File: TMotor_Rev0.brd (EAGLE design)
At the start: 59.7 x 78.4 mm, 37 parts, among them U1 INA125U, U2 INA125U

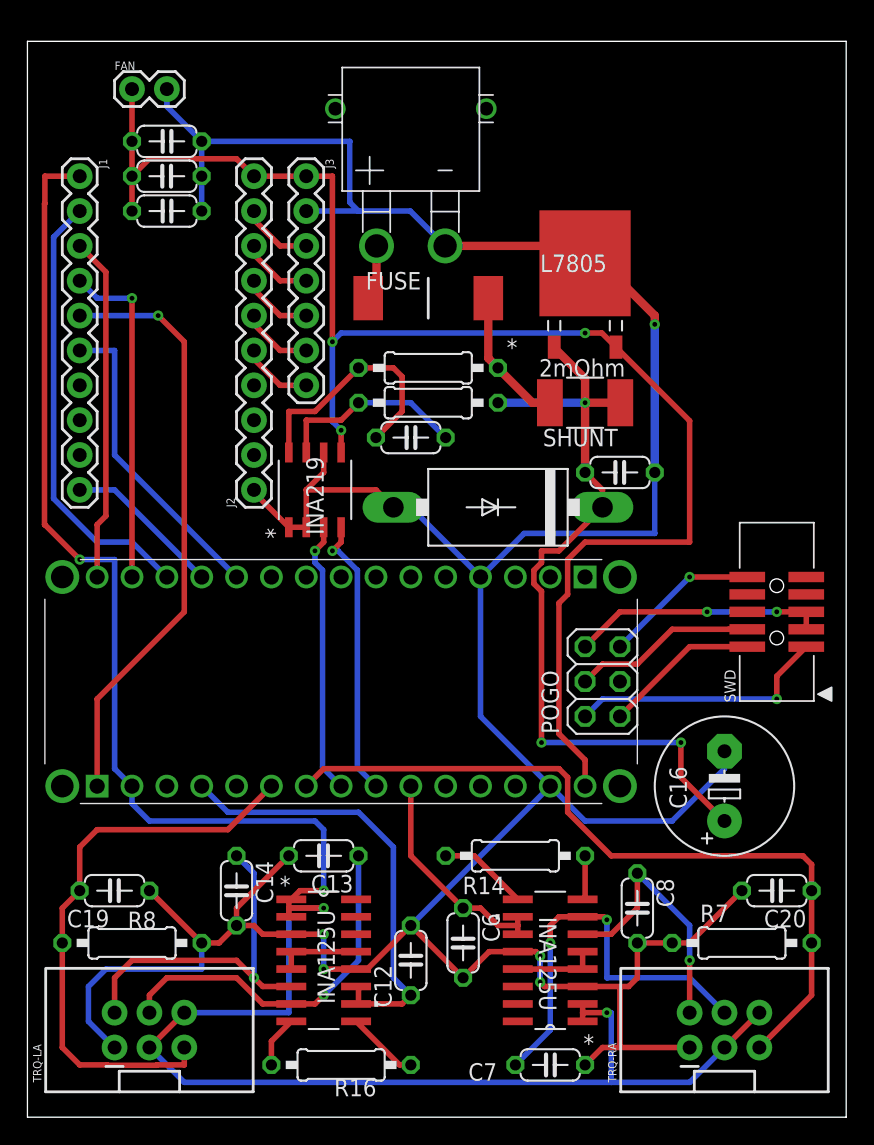
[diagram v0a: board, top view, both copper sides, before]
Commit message: Rearranged pre ground plane pour
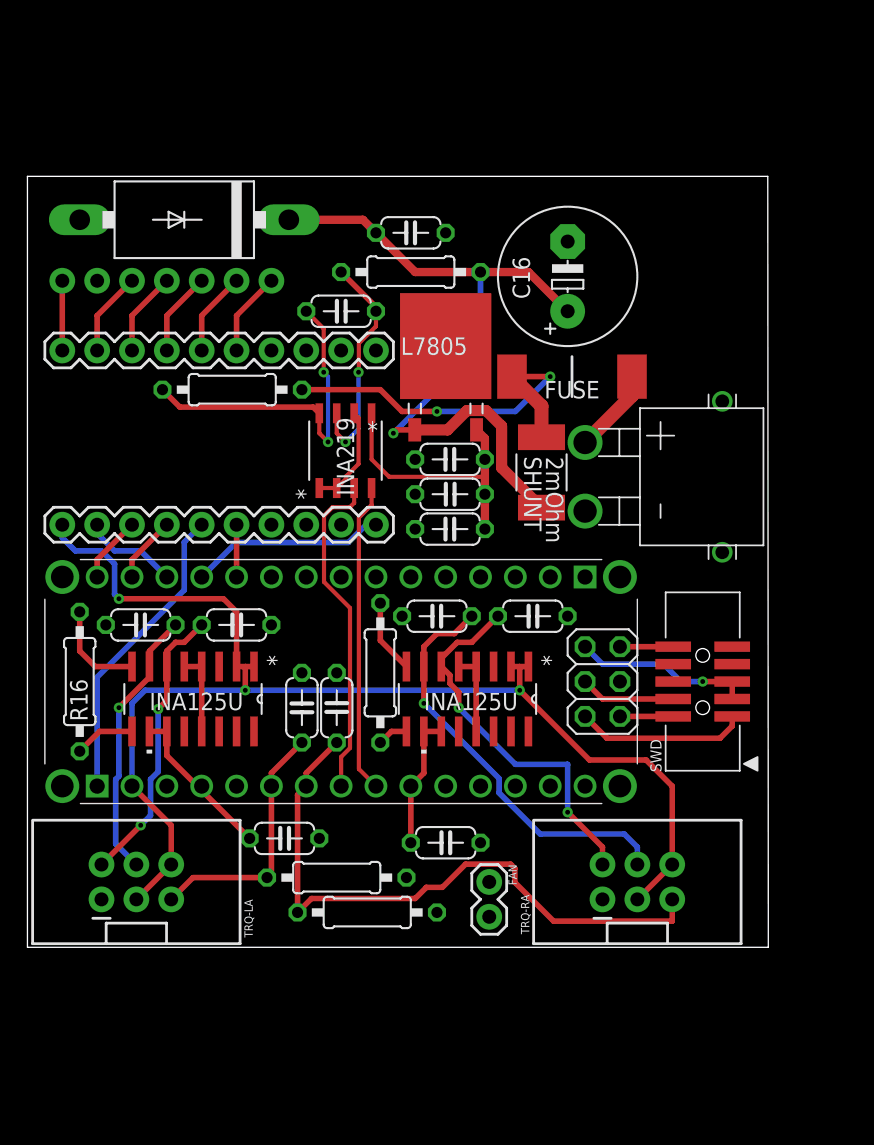
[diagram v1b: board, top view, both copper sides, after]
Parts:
- moved FAN 63.4 mm to (33.7, 13.3), turned to 270 degrees
- moved C16 38.9 mm to (39.4, 57.5)
- moved C20 34.7 mm to (22.5, 26.0), turned to 90 degrees
- moved R16 33.8 mm to (3.81, 27.9), turned to 270 degrees
- moved C7 33.7 mm to (29.8, 32.7), turned to 180 degrees
- moved C15 31.0 mm to (30.8, 44.1), turned to 180 degrees
- moved C3 31.0 mm to (30.8, 41.6), turned to 0 degrees
- moved C5 31.0 mm to (30.8, 39.1), turned to 180 degrees
- moved D1 31.0 mm to (11.4, 61.6)
- moved R7 27.4 mm to (24.8, 11.1), turned to 180 degrees
- moved J1 25.4 mm to (2.54, 39.4), turned to 0 degrees
- moved C4 23.2 mm to (27.9, 60.6)
- moved C8 22.6 mm to (36.8, 32.7), turned to 0 degrees
- moved C13 21.5 mm to (8.26, 32.1)
- moved U1 21.3 mm to (12.1, 26.7), turned to 270 degrees
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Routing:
- net GND: track 260.0 -> 7.51 mm, vias 5 -> 0
- net VIN: track 109.7 -> 24.7 mm, vias 3 -> 0
- net 3.3V: track 155.6 -> 95.7 mm, vias 4 -> 3
- net CAN_CS: track 32.4 -> 7.03 mm
- net A2: track 41.6 -> 18.5 mm
- net SCK: track 43.4 -> 22.2 mm, vias 1 -> 0
- net A0: track 32.7 -> 11.8 mm
- net MISO: track 25.2 -> 4.86 mm
- net MOSI: track 24.7 -> 4.86 mm, vias 1 -> 0
- net CAN_INT: track 22.7 -> 3.81 mm
- net PF_VCC: track 10.2 -> 27.9 mm, vias 0 -> 2
- net A3: track 56.7 -> 46.2 mm
- net N$8: track 19.1 -> 27.5 mm, vias 1 -> 2
- net SWDIO: track 11.4 -> 3.88 mm
- net NRESET: track 11.4 -> 3.88 mm, vias 1 -> 0
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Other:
- board size 59.7 x 78.4 mm -> 54 x 56.2 mm

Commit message: Post ground plane and DRC
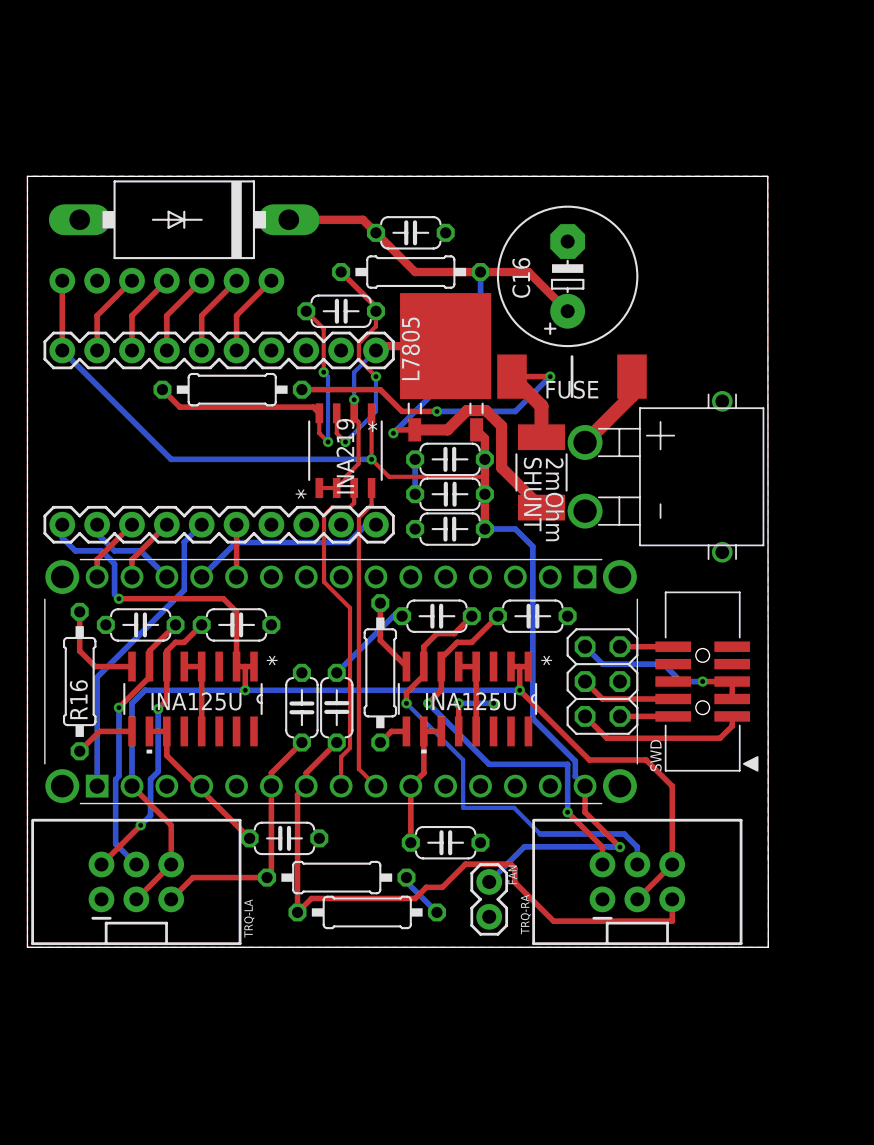
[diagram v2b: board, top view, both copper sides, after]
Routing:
- net VIN: track 24.7 -> 89.7 mm, vias 0 -> 2
- net GND: track 7.51 -> 35.0 mm, vias 0 -> 3
- net N$9: track 30.3 -> 33.8 mm
- net N$8: track 27.5 -> 29.4 mm
- net N$26: track 16.7 -> 17.7 mm
- added copper zone on layer 1, net GND

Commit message: Fixed power electronics, pre Paul PCB changes.
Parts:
- moved C15 27.7 mm to (33.3, 16.5)
- moved L7805 21.5 mm to (51.4, 47.6), turned to 270 degrees
- moved C4 21.2 mm to (47.6, 52.7)
- moved U$9 20.1 mm to (36.8, 62.5), turned to 0 degrees
- moved R2 18.4 mm to (33.0, 52.4)
- moved C5 17.2 mm to (47.6, 42.5), turned to 0 degrees
- moved D1 16.9 mm to (28.3, 63.5), flipped to the bottom, turned to 90 degrees
- moved R1 14.6 mm to (38.1, 47.3)
- moved SHUNT 10.7 mm to (41.0, 53.3)
- moved INA219 10.7 mm to (33.7, 42.5)
- moved C16 10.4 mm to (48.9, 61.6), turned to 0 degrees
- moved C9 9.34 mm to (30.5, 49.5)
- moved FUSE 9.25 mm to (37.1, 59.1), turned to 180 degrees
- moved C3 7.36 mm to (38.1, 42.5), turned to 90 degrees
- moved C6 4.77 mm to (25.7, 16.5)
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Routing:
- net PF_VCC: track 27.9 -> 8.88 mm, vias 2 -> 0
- net L7_VIN: track 53.6 -> 35.4 mm, vias 1 -> 0
- net N$23: track 24.7 -> 8.70 mm, vias 2 -> 0
- net N$26: track 17.7 -> 4.26 mm, vias 2 -> 0
- net GND: track 35.0 -> 22.0 mm, vias 3 -> 2
- net VIN: track 89.7 -> 98.6 mm, vias 2 -> 0
- net SCL1: track 22.6 -> 30.2 mm
- net SDA1: track 24.4 -> 31.8 mm
- net A6: track 9.78 -> 12.0 mm
- net VCC: track 6.22 -> 4.14 mm
- net NRESET: track 3.88 -> 5.89 mm
- net SW3.3V: track 12.5 -> 14.1 mm
- net SWDIO: track 3.88 -> 5.33 mm
- net 3.3V: track 95.7 -> 96.3 mm
- net SCK: track 22.2 -> 22.8 mm
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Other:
- board size 54 x 56.2 mm -> 56.5 x 66.3 mm

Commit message: Forgot to save haha
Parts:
- moved SWD 0.63 mm to (49.8, 31.4)
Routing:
- net SWGND: track 13.4 -> 14.1 mm
- net SWDIO: track 5.33 -> 5.96 mm
- net SWCLK: track 7.34 -> 7.98 mm
- net NRESET: track 5.89 -> 6.52 mm
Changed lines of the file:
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@@
 <attribute name="MOUSER_PRICE-STOCK" value="https://www.mouser.co.uk/ProductDetail/Arduino/ABX00028/?qs=PzGy0jfpSMtit6rnFl8mVg%3D%3D" x="58.42" y="17.78" size="1.778" layer="27" display="off"/>
 </element>
-<element name="SWD" library="microbuilder" package="2X05_1.27MM_BOX_POSTS" value="20317" x="49.2125" y="31.4325" smashed="yes" rot="R90">
-<attribute name="NAME" x="46.2125" y="24.8325" size="0.8128" layer="25" ratio="18" rot="R90"/>
-<attribute name="VALUE" x="51.6125" y="25.3325" size="0.4064" layer="27" ratio="10" rot="R90"/>
+<element name="SWD" library="microbuilder" package="2X05_1.27MM_BOX_POSTS" value="20317" x="49.8475" y="31.4325" smashed="yes" rot="R90">
+<attribute name="NAME" x="46.8475" y="24.8325" size="0.8128" layer="25" ratio="18" rot="R90"/>
+<attribute name="VALUE" x="52.2475" y="25.3325" size="0.4064" layer="27" ratio="10" rot="R90"/>
 </element>
 <element name="POGO" library="pinhead" library_urn="urn:adsk.eagle:library:325" package="2X03" package3d_urn="urn:adsk.eagle:package:22462/2" value="" x="41.91" y="27.94" smashed="yes" rot="R90">
@@
 <contactref element="POGO" pad="4"/>
 <contactref element="SWD" pad="4"/>
-<wire x1="47.0625" y1="30.1625" x2="45.7925" y2="30.1625" width="0.4064" layer="1"/>
+<wire x1="47.6975" y1="30.1625" x2="45.7925" y2="30.1625" width="0.4064" layer="1"/>
 <wire x1="45.7925" y1="30.1625" x2="44.84" y2="29.21" width="0.4064" layer="1"/>
 <wire x1="44.84" y1="29.21" x2="41.91" y2="29.21" width="0.4064" layer="1"/>
@@
 <contactref element="SWD" pad="5"/>
 <wire x1="40.64" y1="30.48" x2="41.91" y2="29.21" width="0.4064" layer="16"/>
-<wire x1="49.2125" y1="31.4325" x2="47.625" y2="31.4325" width="0.4064" layer="16"/>
+<wire x1="49.8475" y1="31.4325" x2="47.625" y2="31.4325" width="0.4064" layer="16"/>
 <wire x1="47.625" y1="31.4325" x2="45.4025" y2="29.21" width="0.4064" layer="16"/>
 <wire x1="45.4025" y1="29.21" x2="41.91" y2="29.21" width="0.4064" layer="16"/>
-<via x="49.2125" y="31.4325" extent="1-16" drill="0.35"/>
-<wire x1="51.3625" y1="31.4325" x2="49.2125" y2="31.4325" width="0.4064" layer="1"/>
-<wire x1="51.3625" y1="31.4325" x2="51.3625" y2="30.1625" width="0.4064" layer="1"/>
+<via x="49.8475" y="31.4325" extent="1-16" drill="0.35"/>
+<wire x1="51.9975" y1="31.4325" x2="49.8475" y2="31.4325" width="0.4064" layer="1"/>
+<wire x1="51.9975" y1="31.4325" x2="51.9975" y2="30.1625" width="0.4064" layer="1"/>
 </signal>
 <signal name="SW3.3V">
@@
 <wire x1="40.64" y1="25.4" x2="42.2275" y2="23.8125" width="0.4064" layer="1"/>
 <wire x1="42.2275" y1="23.8125" x2="47.3075" y2="23.8125" width="0.4064" layer="1"/>
-<wire x1="47.3075" y1="23.8125" x2="51.3625" y2="27.8675" width="0.4064" layer="1"/>
-<wire x1="51.3625" y1="27.8675" x2="51.3625" y2="28.8925" width="0.4064" layer="1"/>
+<wire x1="47.3075" y1="23.8125" x2="51.9975" y2="28.5025" width="0.4064" layer="1"/>
+<wire x1="51.9975" y1="28.5025" x2="51.9975" y2="28.8925" width="0.4064" layer="1"/>
 </signal>
 <signal name="NRESET">
 <contactref element="POGO" pad="5"/>
 <contactref element="SWD" pad="10"/>
-<wire x1="47.0625" y1="33.9725" x2="45.72" y2="33.9725" width="0.4064" layer="1"/>
+<wire x1="47.6975" y1="33.9725" x2="45.72" y2="33.9725" width="0.4064" layer="1"/>
 <wire x1="45.72" y1="33.9725" x2="43.18" y2="31.4325" width="0.4064" layer="1"/>
 <wire x1="43.18" y1="30.48" x2="43.18" y2="31.4325" width="0.4064" layer="1"/>
@@
 <contactref element="POGO" pad="1"/>
 <contactref element="SWD" pad="2"/>
-<wire x1="47.0625" y1="28.8925" x2="46.6725" y2="28.8925" width="0.4064" layer="1"/>
+<wire x1="47.6975" y1="28.8925" x2="46.6725" y2="28.8925" width="0.4064" layer="1"/>
 <wire x1="43.18" y1="25.4" x2="46.6725" y2="28.8925" width="0.4064" layer="1"/>
 </signal>

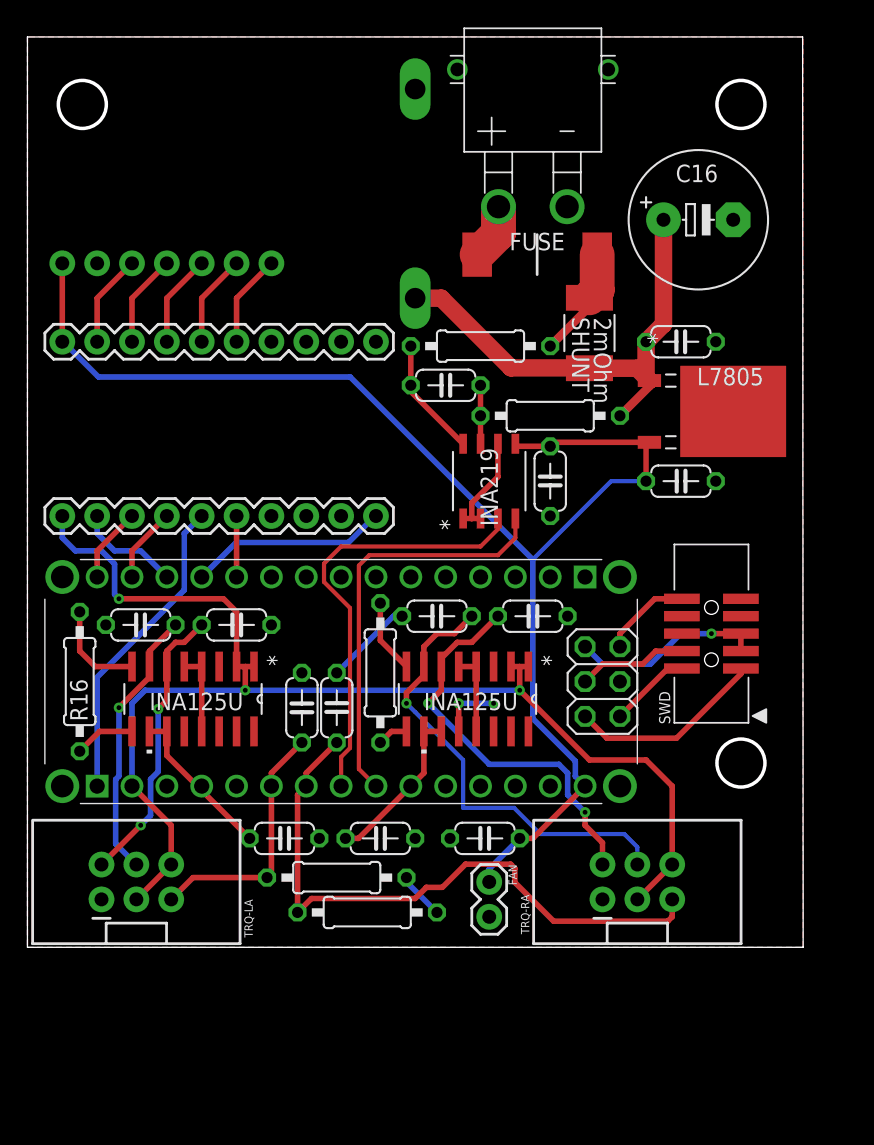
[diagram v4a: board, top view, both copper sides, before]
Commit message: Added silkscreen and finalized design
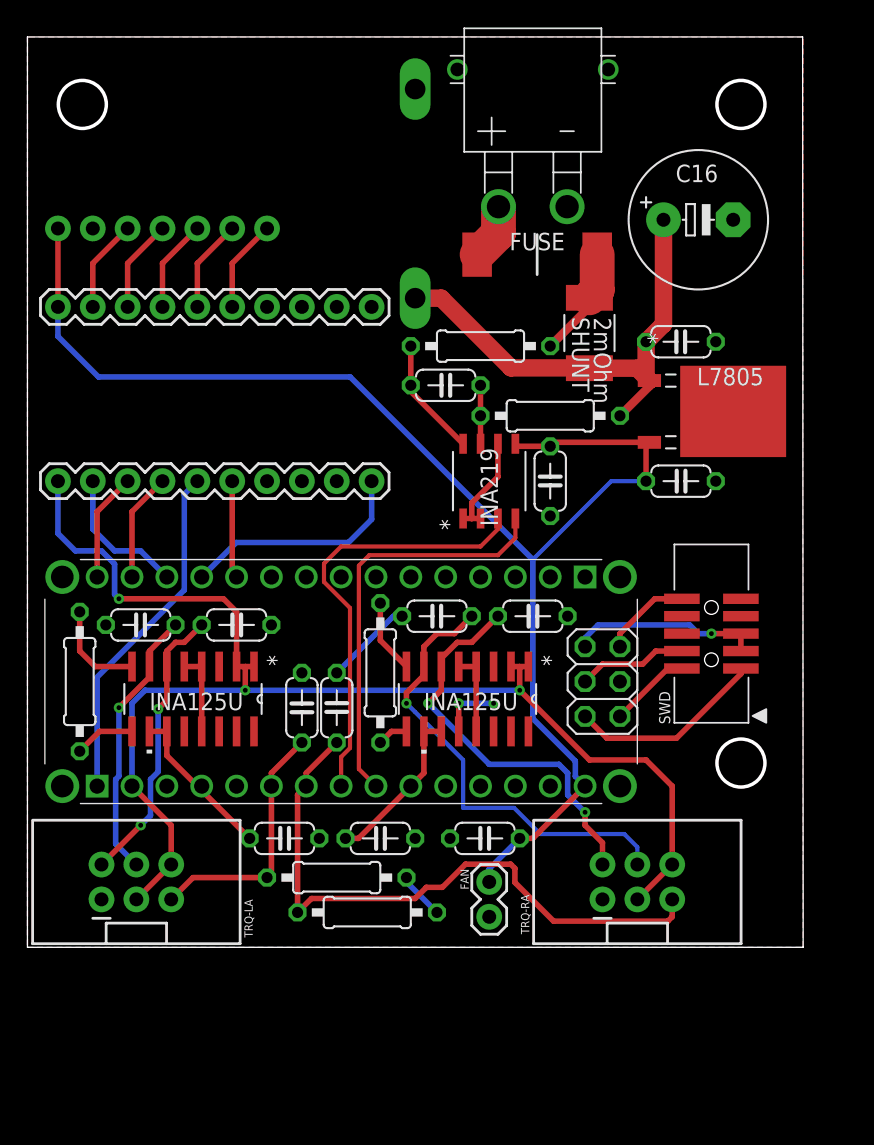
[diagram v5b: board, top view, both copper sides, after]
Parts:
- moved J1 2.56 mm to (2.22, 42.5)
- moved J2 2.56 mm to (25.1, 55.2)
- moved J3 2.56 mm to (2.22, 61.0)
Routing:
- net CAN_INT: track 4.45 -> 7.12 mm
- net CAN_CS: track 7.67 -> 10.3 mm
- net 3.3V: track 96.3 -> 99.0 mm
- net VIN: track 98.6 -> 101.2 mm
- net SCK: track 22.8 -> 25.2 mm
- net MISO: track 5.50 -> 7.91 mm
- net MOSI: track 5.50 -> 7.91 mm
- net LLS_OE: track 14.5 -> 16.9 mm
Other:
- board text added: "AK_Board V0"
- board text added: "CAN"
- board text added: "LLS"

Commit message: Final V0 sent to oshpark
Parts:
- R14: value 3.3k -> 470R
- R16: value 1k -> 470R
- moved J3 0.32 mm to (2.22, 61.3), flipped to the top, turned to 0 degrees
- flipped D1 to the top
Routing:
- net GND: track 22.0 -> 15.6 mm
- net 3.3V: track 99.0 -> 99.6 mm
- net N$9: track 33.5 -> 33.0 mm
